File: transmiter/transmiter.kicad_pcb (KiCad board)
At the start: 2 copper layers, 54.4 x 48.3 mm, 64 parts, among them J1 USB_B_Mini, J2 Conn_01x04_Pin, J3 Conn_01x04_Pin, SW1 SW_Push, SW2 SW_SPDT, U1 ADL5370, U2 STM32F303K8Tx, U3 AMS1117-3.3, U4 ADL5531, U5 Si590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

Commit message: Finished PCB design
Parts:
- removed C27: C, Capacitor_SMD:C_0402_1005Metric_Pad0.74x0.62mm_HandSolder
- removed U5: Si590, Oscillator:Oscillator_SMD_IDT_JU6-6_7.0x5.0mm_P2.54mm
- added C32: C, Capacitor_SMD:C_0603_1608Metric_Pad1.08x0.95mm_HandSolder, F.Cu at (92.3, 92.3)
- added C33: C, Capacitor_SMD:C_0603_1608Metric_Pad1.08x0.95mm_HandSolder, F.Cu at (93.1, 98.7)
- added C34: C, Capacitor_SMD:C_0603_1608Metric_Pad1.08x0.95mm_HandSolder, F.Cu at (97.7, 96.7)
- added H1: MountingHole_Pad, MountingHole:MountingHole_2.2mm_M2_DIN965_Pad, F.Cu at (85.5, 54.5)
- added H2: MountingHole_Pad, MountingHole:MountingHole_2.2mm_M2_DIN965_Pad, F.Cu at (133.5, 54.5)
- added H3: MountingHole_Pad, MountingHole:MountingHole_2.2mm_M2_DIN965_Pad, F.Cu at (133.5, 99.5)
- added H4: MountingHole_Pad, MountingHole:MountingHole_2.2mm_M2_DIN965_Pad, F.Cu at (85.5, 99.5)
- added L6: 18n, Inductor_SMD:L_0603_1608Metric_Pad1.05x0.95mm_HandSolder, F.Cu at (95.0, 91.4)
- added R11: 1.5k, Resistor_SMD:R_0603_1608Metric_Pad0.98x0.95mm_HandSolder, F.Cu at (125.3, 60.7)
- added R12: 1k, Resistor_SMD:R_0603_1608Metric_Pad0.98x0.95mm_HandSolder, F.Cu at (96.6, 98.7)
- added U8: STM32F303K8Tx, Package_QFP:LQFP-32_7x7mm_P0.8mm, F.Cu at (103.9, 69.0)
- AE2: footprint Connector_Coaxial:U.FL_Hirose_U.FL-R-SMT-1_Vertical -> Connector_Coaxial:U.FL_Molex_MCRF_73412-0110_Vertical
- U2: value STM32F303K8Tx -> MAX2608; footprint Package_QFP:LQFP-32_7x7mm_P0.8mm -> Package_TO_SOT_SMD:SOT-23-6
- moved U2 28.3 mm to (94.0, 95.6), turned to -90 degrees
- moved C31 12.1 mm to (114.8, 63.0), turned to -90 degrees
- moved C29 9.97 mm to (113.9, 66.0), turned to 0 degrees
- moved R10 9.25 mm to (122.4, 56.7), turned to -90 degrees
- moved D2 9.17 mm to (118.5, 61.2)
- moved D3 9.16 mm to (118.6, 58.9)
- moved C30 9.03 mm to (113.9, 67.5), turned to 0 degrees
- moved C26 8.53 mm to (116.6, 92.6)
- moved AE2 8.46 mm to (119.8, 96.6), turned to 180 degrees
- moved R4 8.28 mm to (124.4, 56.7), turned to -90 degrees
- moved L5 7.52 mm to (113.0, 91.4)
- moved R1 6.29 mm to (95.7, 60.6), turned to 0 degrees
- moved U9 5.06 mm to (120.8, 68.5)
- moved C22 4.82 mm to (116.0, 95.5), turned to -90 degrees
- moved C7 3.69 mm to (109.4, 75.1), turned to 180 degrees
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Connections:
- net Net-(U9-3V3OUT) renamed 3V3
- C29 pad 2: +3V3 -> +5V
- C30 pad 2: +3V3 -> +5V
- U2 pad 1: +3V3 -> Net-(U2-IND)
- U2 pad 2: HSE_IN -> Net-(U2-TUNE)
- U2 pad 3: HSE_OUT -> GND
- U2 pad 4: NRST -> unconnected-(U2-OUT--Pad4)
- U2 pad 5: +3VA3 -> +5V
- U2 pad 6: unconnected-(U2-PA0-Pad6) -> Net-(U2-OUT+)
- U9 pad 11: USART1_RTS -> unconnected-(U9-CTS-Pad11)
- U9 pad 20: +3V3 -> +5V
- U9 pad 26: unconnected-(U9-TEST-Pad26) -> GND
- U9 pad 3: USART1_CTS -> unconnected-(U9-RTS-Pad3)
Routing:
- net +5V: track 36.1 -> 103.8 mm, vias 0 -> 2
- net 3V3: track 2.32 -> 39.6 mm
- net GND: track 0.00 -> 37.1 mm, vias 0 -> 47
- net +3V3: track 210.2 -> 191.9 mm
- net USART1_CTS: track 12.2 -> 0.00 mm
- net USART1_RX: track 24.6 -> 34.9 mm
- net USART1_TX: track 33.8 -> 43.2 mm
- net Net-(SW2-B): track 9.93 -> 2.83 mm
- net Net-(D2-A): track 0.00 -> 6.94 mm
- net BOOT: track 2.01 -> 8.39 mm
- net USB_D+: track 13.3 -> 19.7 mm
- net USB_D-: track 13.3 -> 19.7 mm
- net LOIP: track 6.48 -> 1.46 mm
- net Net-(U2-OUT+): track 0.00 -> 4.12 mm
- net Net-(D3-A): track 0.00 -> 3.71 mm
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- added copper zone on B.Cu, net GND
- added copper zone on F.Cu, net GND
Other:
- board size 54.4 x 48.3 mm -> 55 x 52 mm
- board text added: "SWD"
- board text added: "UART"

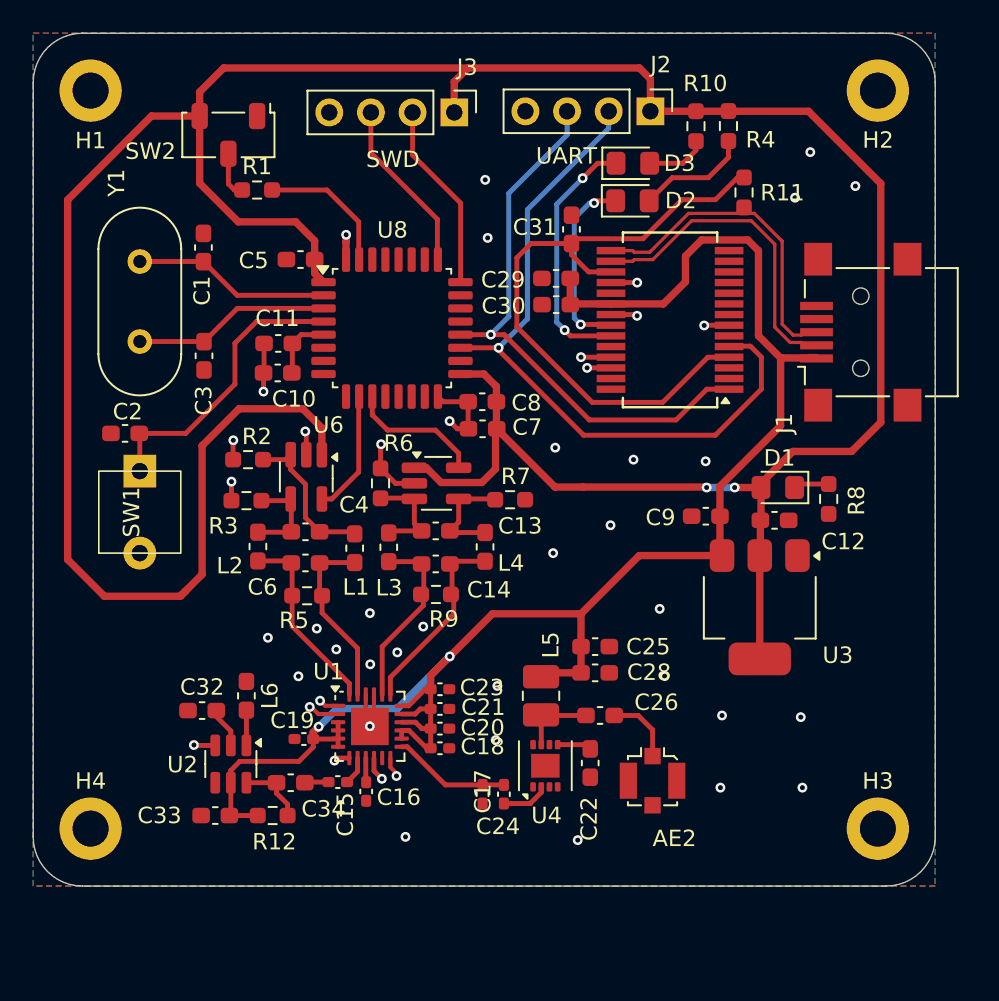
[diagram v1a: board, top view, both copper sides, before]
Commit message: First design of sended PCBs
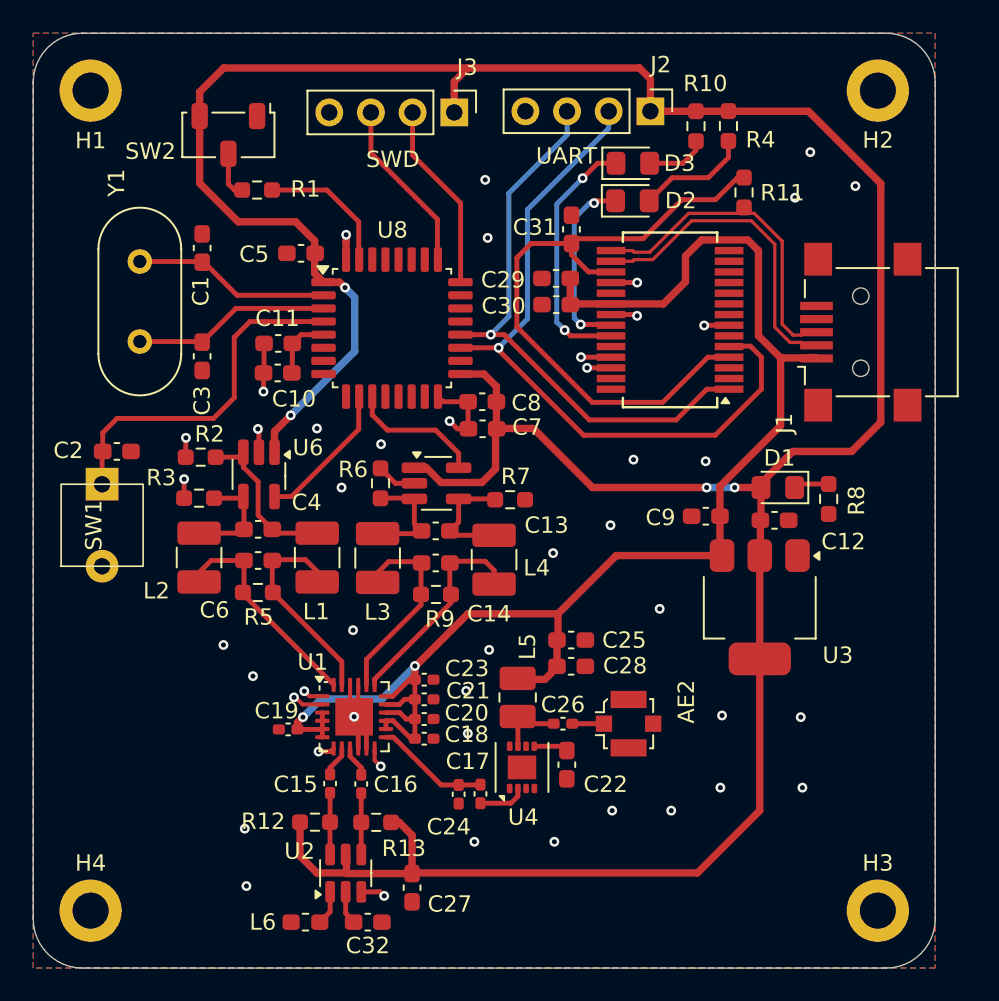
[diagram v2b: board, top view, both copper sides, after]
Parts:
- removed C33, C34: C, Capacitor_SMD:C_0603_1608Metric_Pad1.08x0.95mm_HandSolder
- added C27: C, Capacitor_SMD:C_0603_1608Metric_Pad1.08x0.95mm_HandSolder, F.Cu at (105.1, 103.1)
- added R13: 1k, Resistor_SMD:R_0603_1608Metric_Pad0.98x0.95mm_HandSolder, F.Cu at (102.9, 99.1)
- C26: footprint Capacitor_SMD:C_0603_1608Metric_Pad1.08x0.95mm_HandSolder -> Capacitor_SMD:C_0402_1005Metric_Pad0.74x0.62mm_HandSolder
- L1, L2, L3, L4: footprint Inductor_SMD:L_0603_1608Metric_Pad1.05x0.95mm_HandSolder -> Inductor_SMD:L_1210_3225Metric_Pad1.42x2.65mm_HandSolder
- moved C32 16.4 mm to (102.4, 105.2), turned to 180 degrees
- moved L6 14.3 mm to (98.6, 105.2), turned to 0 degrees
- moved U2 9.66 mm to (101.1, 102.2), turned to 90 degrees
- moved H3 5.00 mm to (133.5, 104.5)
- moved H4 5.00 mm to (85.5, 104.5)
- moved AE2 3.77 mm to (118.3, 93.1), turned to -90 degrees
- moved L2 3.65 mm to (92.1, 83.0)
- moved R5 3.01 mm to (95.7, 85.1)
- moved R3 2.89 mm to (92.1, 79.3)
- moved U6 2.89 mm to (95.8, 77.9)
- moved C4 2.89 mm to (95.7, 81.2)
- moved R2 2.89 mm to (92.2, 76.8)
- moved C6 2.89 mm to (95.7, 83.2)
- moved R12 2.61 mm to (99.2, 99.1)
- moved SW1 2.44 mm to (86.2, 81.0)
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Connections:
- C15 pad 2: LOIP -> LO_P
- C16 pad 2: GND -> LO_N
- R12 pad 1: +5V -> +3V3
- R12 pad 2: Net-(U2-OUT+) -> LO_P
- U2 pad 4: unconnected-(U2-OUT--Pad4) -> LO_N
- U2 pad 5: +5V -> +3V3
- U2 pad 6: Net-(U2-OUT+) -> LO_P
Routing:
- net +5V: track 103.8 -> 92.2 mm
- net Net-(U2-OUT+): track 4.12 -> 0.00 mm
- net NRST: track 17.8 -> 21.9 mm
- net LO_P: track 0.00 -> 3.76 mm
- net LO_N: track 0.00 -> 3.74 mm
- net Net-(AE2-A): track 4.30 -> 1.63 mm
- net QBBN: track 10.9 -> 13.1 mm
- net QBBP: track 11.6 -> 13.5 mm
- net GND: track 37.1 -> 39.0 mm, vias 47 -> 46
- net IBBN: track 10.9 -> 12.5 mm
- net LOIP: track 1.46 -> 0.00 mm
- net IBBP: track 11.9 -> 13.4 mm
- net DAC1_OUT1: track 7.53 -> 8.83 mm
- net Net-(U6-D_OUT-): track 9.25 -> 10.1 mm
- net Net-(U6-D_OUT+): track 5.89 -> 6.68 mm
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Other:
- board size 55 x 52 mm -> 55 x 57 mm
- board text added: "REF**"
